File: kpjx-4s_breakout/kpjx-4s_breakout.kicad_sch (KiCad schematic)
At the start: 10 parts, among them J1 Conn_01x09, J2 Conn_01x08_Male, J3 Conn_02x04_Odd_Even, J4 Conn_02x04_Odd_Even, J5 Conn_02x04_Odd_Even, J6 Conn_02x04_Odd_Even

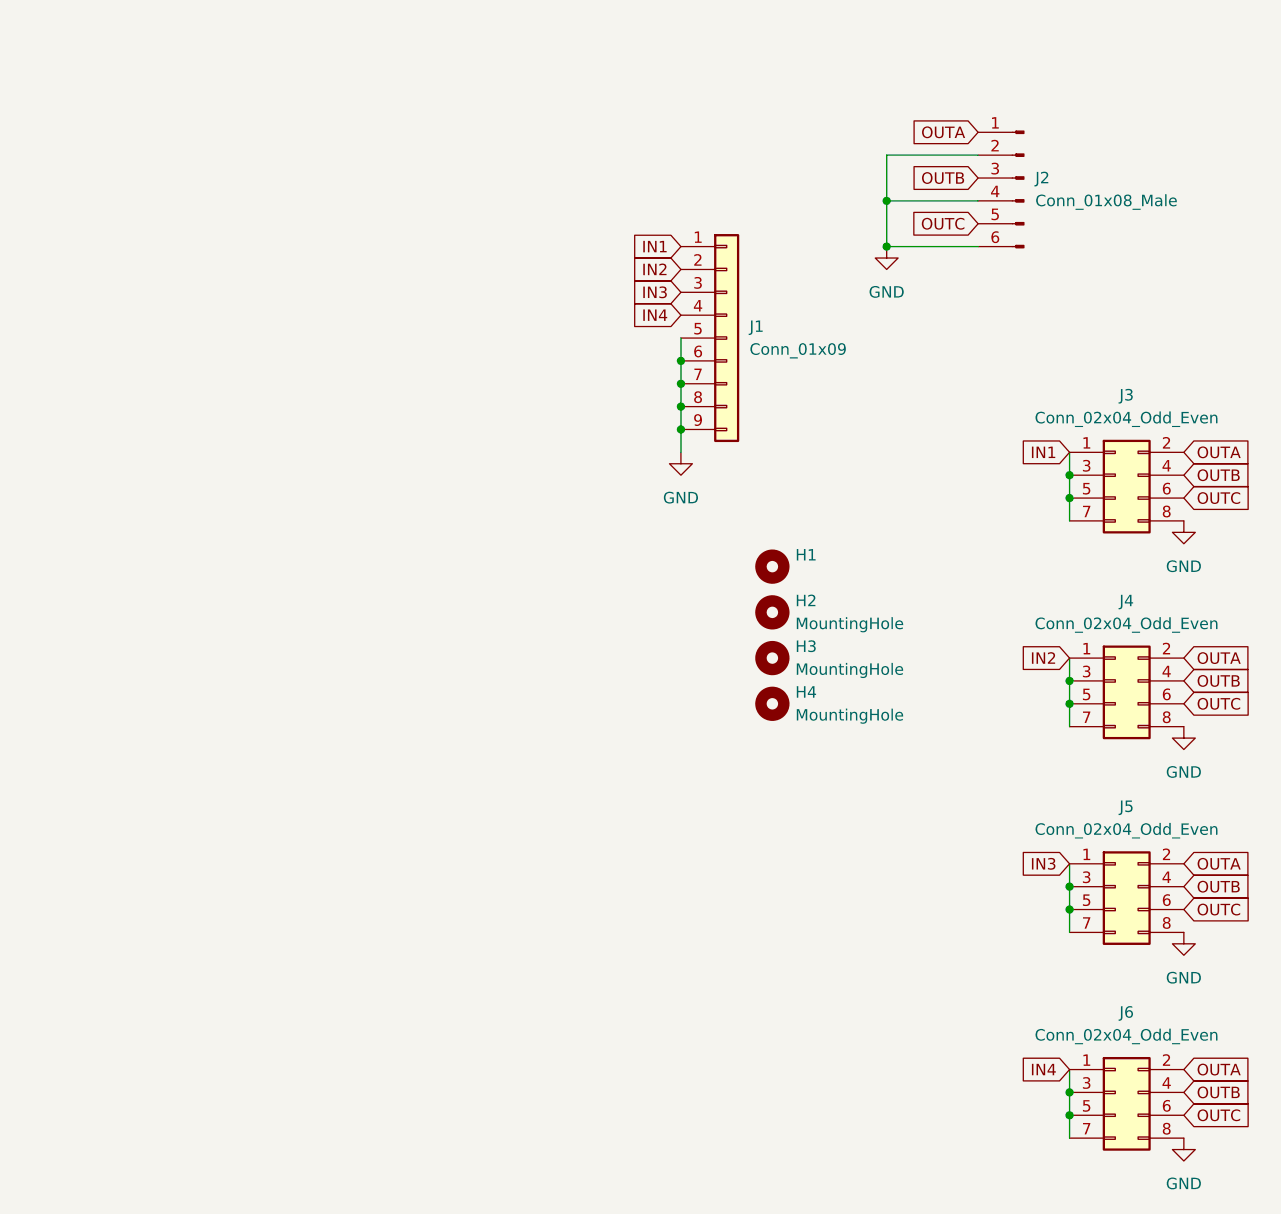
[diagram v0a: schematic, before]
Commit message: Add pictures, clean up schematic
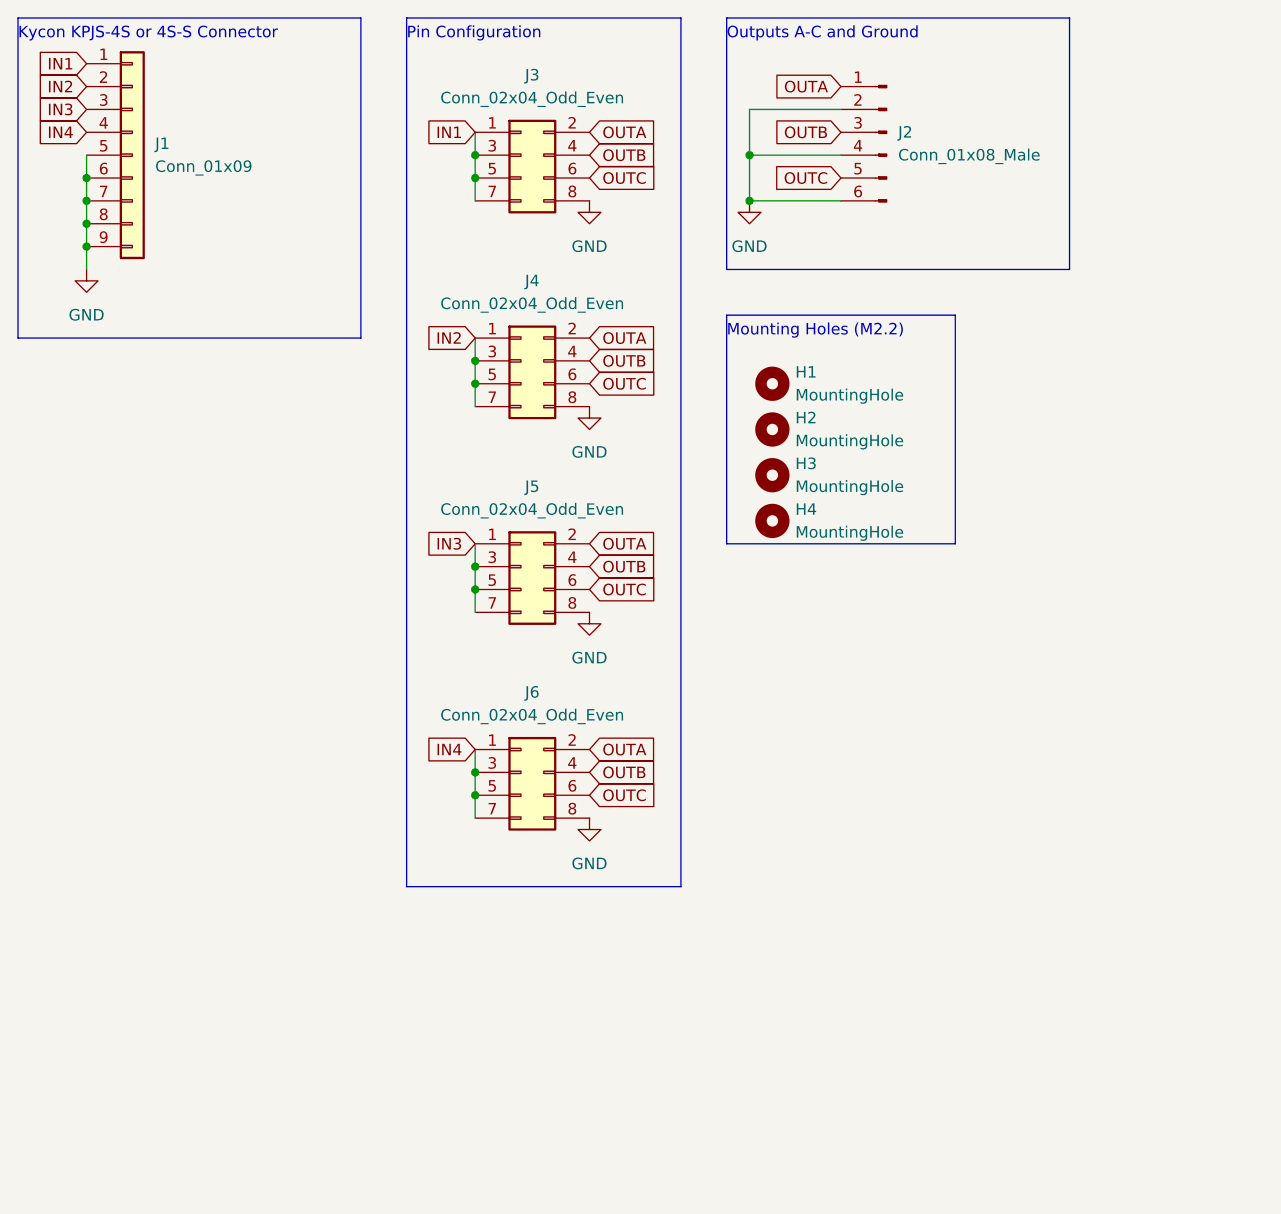
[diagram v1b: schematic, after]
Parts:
- H1: value (none) -> MountingHole; footprint (none) -> MountingHole:MountingHole_2.2mm_M2_DIN965
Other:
- note added: "Kycon KPJS-4S or 4S-S Connector"
- note added: "Mounting Holes (M2.2)"
- note added: "Outputs A-C and Ground"
- note added: "Pin Configuration"
- company: (none) -> Matthew Nielsen (xunker)
- title: (none) -> Kycon KPJX-4S Breakout
- moved on the sheet: H1, H2, H3, H4, J1, J2, J3, J4, J5, J6
